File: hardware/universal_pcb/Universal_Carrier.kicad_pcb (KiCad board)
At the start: 2 copper layers, 100 x 85 mm, 20 parts, among them J1 ESP32_T_LANDSCAPE, J11 PWR_ESP_5V, J12 PWR_SERVO_5V, J2 ESP32_B_LANDSCAPE, J3 SX1278_LORA_2x4, J4 BATT_APM, J5 DETECTOR_ANCORA, J6 GPS_LC29H_7PIN, SW1 subir ancora, SW2 MODE, SW3 largar ancora, SW4 BOOT

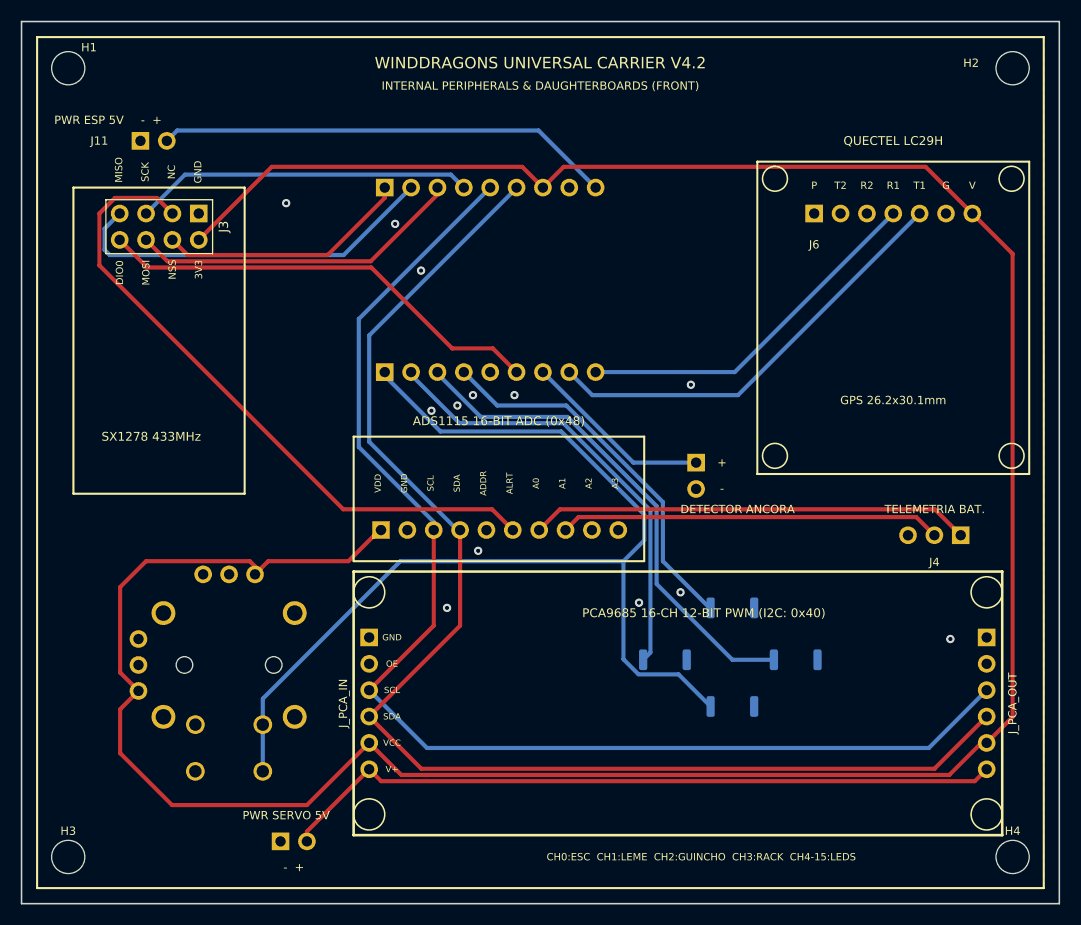
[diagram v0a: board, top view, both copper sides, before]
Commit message: feat: update Universal Carrier PCB design and gerber files with I2C cleanup
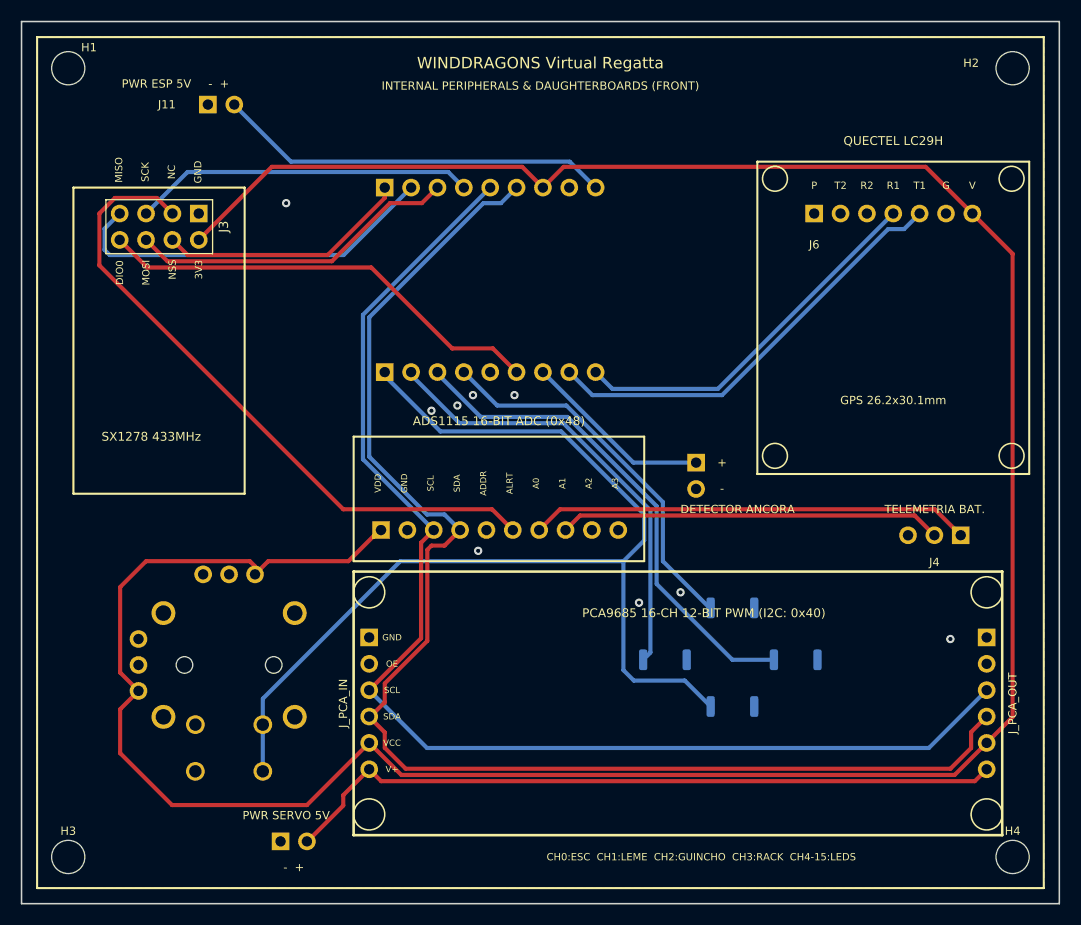
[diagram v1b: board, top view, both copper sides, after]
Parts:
- added LOGO1: WindDragons_Logo, WindDragons:WindDragons_Logo_20mm, B.Cu at (83.0, 32.5)
- moved J11 7.38 mm to (18.0, 8.00)
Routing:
- net /+5V: track 44.0 -> 38.2 mm
- net /I2C_SDA: track 127.9 -> 132.4 mm
- net /IO17_GPS_TX: track 35.0 -> 36.4 mm
- net /IO9_BOOT: track 103.7 -> 104.3 mm
- net /GND: vias 13 -> 9
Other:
- board text added: "WINDDRAGONS Virtual Regatta"
- board text added: "WINDDRAGONS virtual Regatta V1.0"
- board text removed: "USER INTERFACE: DISPLAY & PS5 JOYSTICK"
- board text removed: "WINDDRAGONS REMOTE CONTROL & CARRIER V4.2"
- board text removed: "WINDDRAGONS UNIVERSAL CARRIER V4.2"

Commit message: refactor: update base display screens and simplify navigation pages
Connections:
- J2 pad 5: /IO23_SPARE -> /IO23_LORA_DIO0
- J2 pad 6: /IO12_LORA_DIO0 -> /IO12_USB_DM
- J3 pad 8: /IO12_LORA_DIO0 -> /IO23_LORA_DIO0
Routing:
- net /IO12_LORA_DIO0: track 43.5 -> 0.00 mm
- net /IO23_LORA_DIO0: track 0.00 -> 41.0 mm
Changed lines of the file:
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@@
 			(layers "*.Cu" "*.Mask" "F.SilkS")
 			(remove_unused_layers no)
-			(net "/IO12_LORA_DIO0")
+			(net "/IO23_LORA_DIO0")
 		)
 		(embedded_fonts no)
@@
 			(layers "*.Cu" "*.Mask" "B.SilkS")
 			(remove_unused_layers no)
-			(net "/IO23_SPARE")
+			(net "/IO23_LORA_DIO0")
 		)
 		(pad "6" thru_hole circle
@@
 			(layers "*.Cu" "*.Mask" "B.SilkS")
 			(remove_unused_layers no)
-			(net "/IO12_LORA_DIO0")
+			(net "/IO12_USB_DM")
 		)
 		(pad "7" thru_hole circle
@@
 		(width 0.4)
 		(layer "F.Cu")
-		(net "/IO12_LORA_DIO0")
+		(net "/IO23_LORA_DIO0")
 	)
 	(segment
@@
 		(width 0.4)
 		(layer "F.Cu")
-		(net "/IO12_LORA_DIO0")
+		(net "/IO23_LORA_DIO0")
 	)
 	(segment
-		(start 47.7 33.78)
-		(end 45.42 31.5)
+		(start 45.16 33.78)
+		(end 42.88 31.5)
 		(width 0.4)
 		(layer "F.Cu")
-		(net "/IO12_LORA_DIO0")
+		(net "/IO23_LORA_DIO0")
 	)
 	(segment
@@
 		(width 0.4)
 		(layer "F.Cu")
-		(net "/IO12_LORA_DIO0")
+		(net "/IO23_LORA_DIO0")
 	)
 	(segment
-		(start 45.42 31.5)
+		(start 42.88 31.5)
 		(end 41.5 31.5)
 		(width 0.4)
 		(layer "F.Cu")
-		(net "/IO12_LORA_DIO0")
+		(net "/IO23_LORA_DIO0")
 	)
 	(segment
